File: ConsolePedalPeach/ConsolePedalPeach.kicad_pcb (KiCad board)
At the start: 2 copper layers, 100 x 60 mm, 34 parts, among them J1 Conn_02x25_Counter_Clockwise, U1 TL072, U2 LM386, U3 LM386

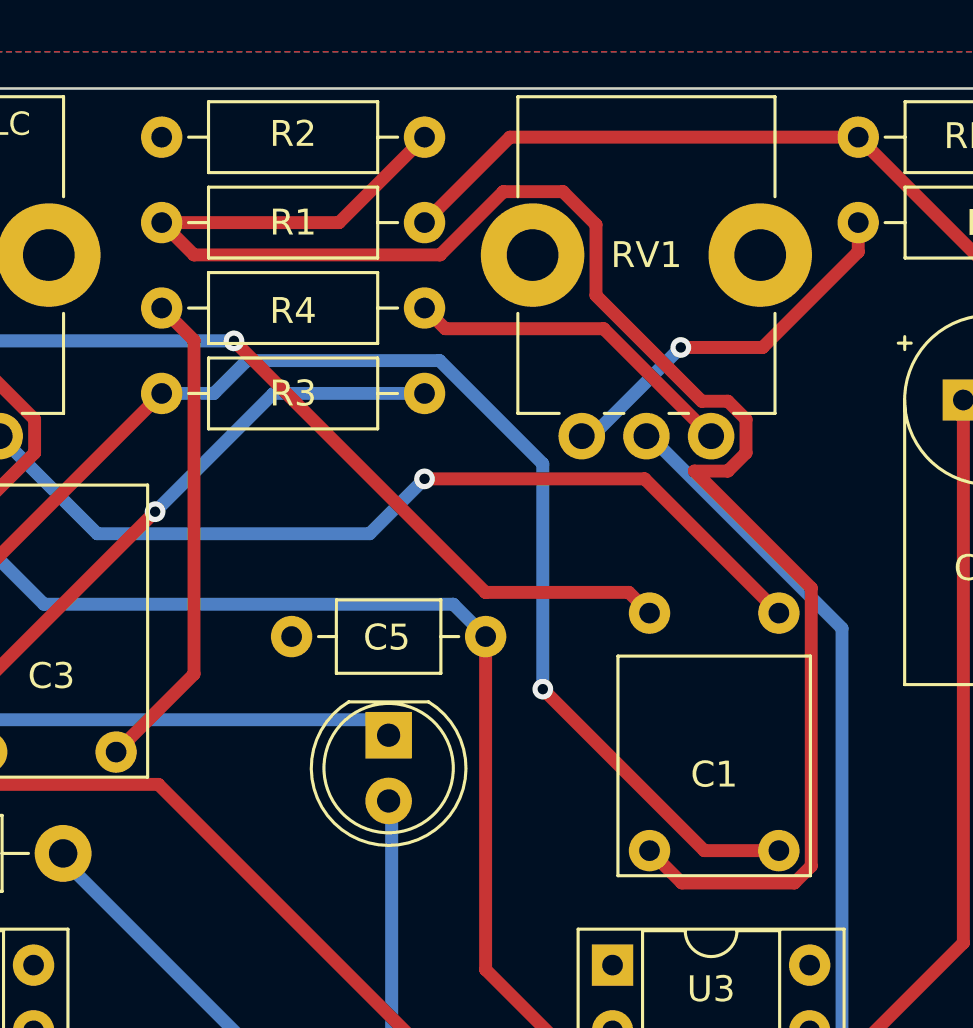
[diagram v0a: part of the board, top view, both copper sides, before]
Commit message: Fixed bad autoroute and replotted gerbers
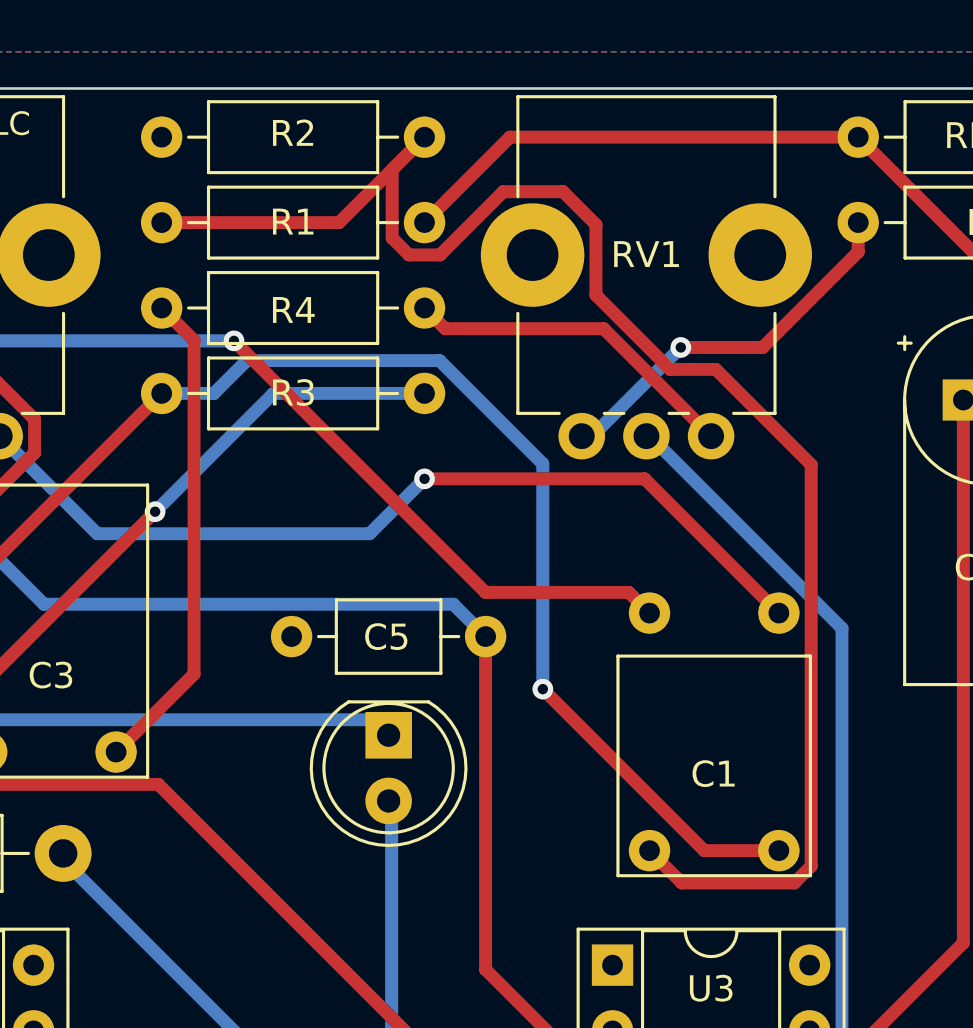
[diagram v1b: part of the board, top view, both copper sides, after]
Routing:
- net Net-(C1-Pad2): track 68.7 -> 61.9 mm
